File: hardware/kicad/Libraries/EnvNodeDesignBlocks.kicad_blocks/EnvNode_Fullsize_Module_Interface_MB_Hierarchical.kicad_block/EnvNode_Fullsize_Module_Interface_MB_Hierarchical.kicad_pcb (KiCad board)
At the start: 2 copper layers, 2 parts, among them J1 Conn_02x04_Odd_Even, J2 Conn_02x04_Odd_Even

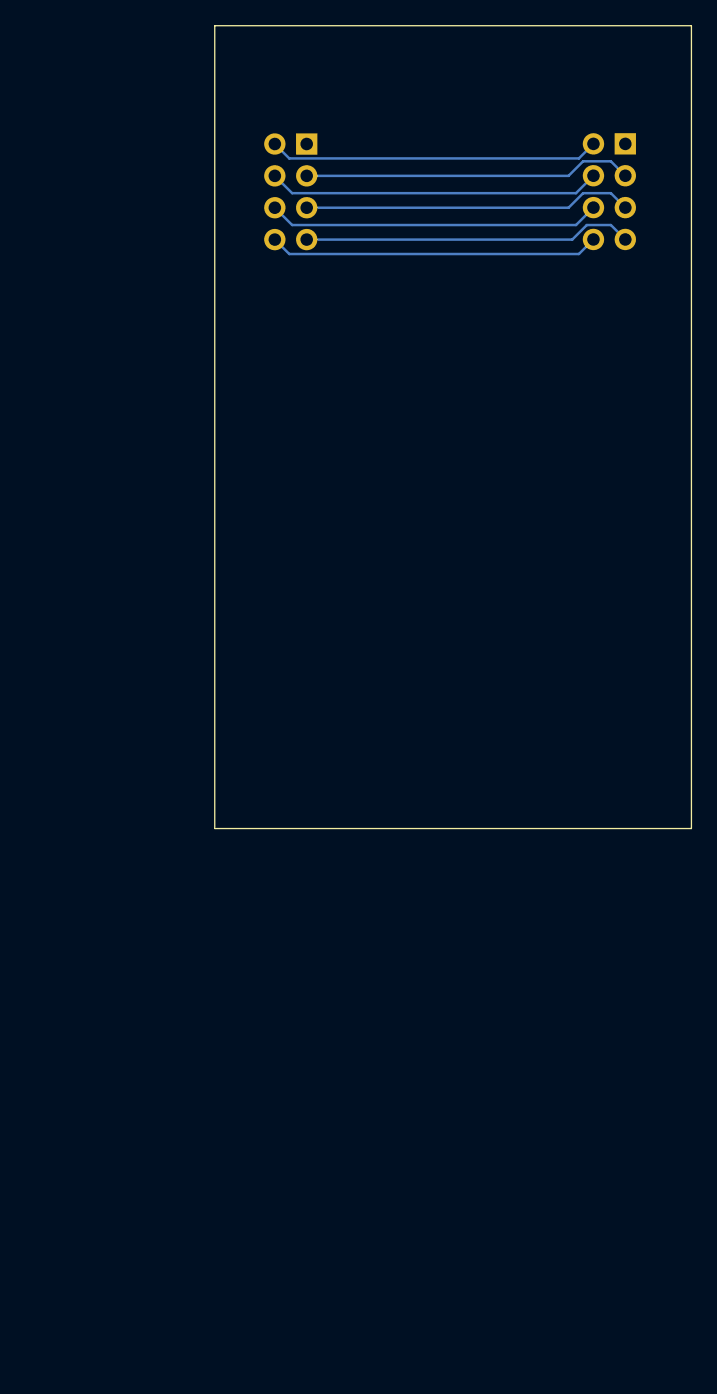
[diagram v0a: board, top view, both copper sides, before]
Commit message: Updated EnvNode Modules Interfaces
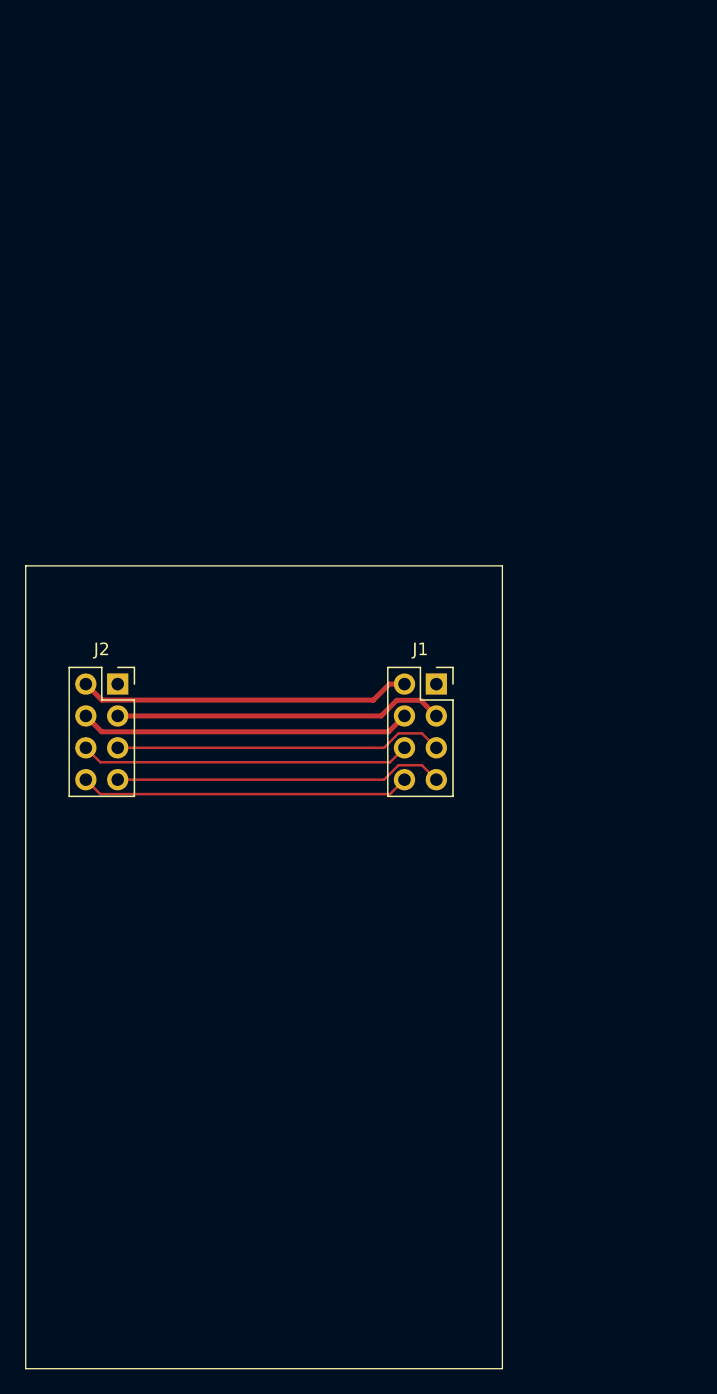
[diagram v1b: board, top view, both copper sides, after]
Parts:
- J1, J2: footprint EnvNode-Footprints:PinSocket_2x04_P2.54mm_Vertical_Bottom -> Connector_PinSocket_2.54mm:PinSocket_2x04_P2.54mm_Vertical; moved to F.Cu
- moved J1 44.8 mm to (171.2, 87.4), turned to 0 degrees
- moved J2 44.8 mm to (145.8, 87.4), turned to 0 degrees
